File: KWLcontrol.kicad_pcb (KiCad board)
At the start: 2 copper layers, 56.4 x 38.5 mm, 33 parts, among them J1 Conn_01x03_Pin, J2 Conn_01x03_Socket, J3 Conn_01x03, U1 ESP32-WROOM-32, U2 TPS62172DSG, U3 TPS62172DSG, U4 TXS0101DBV

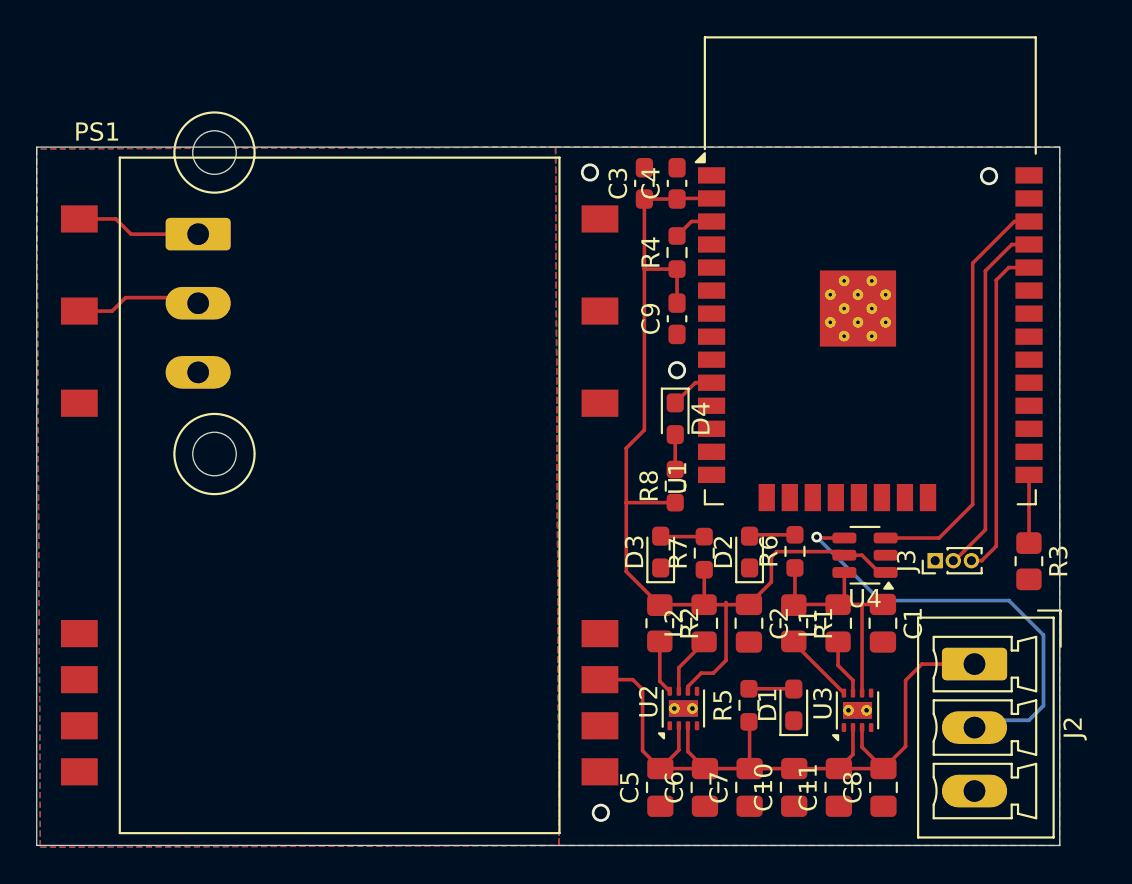
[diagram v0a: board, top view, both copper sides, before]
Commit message: new connectors, some silkscreen
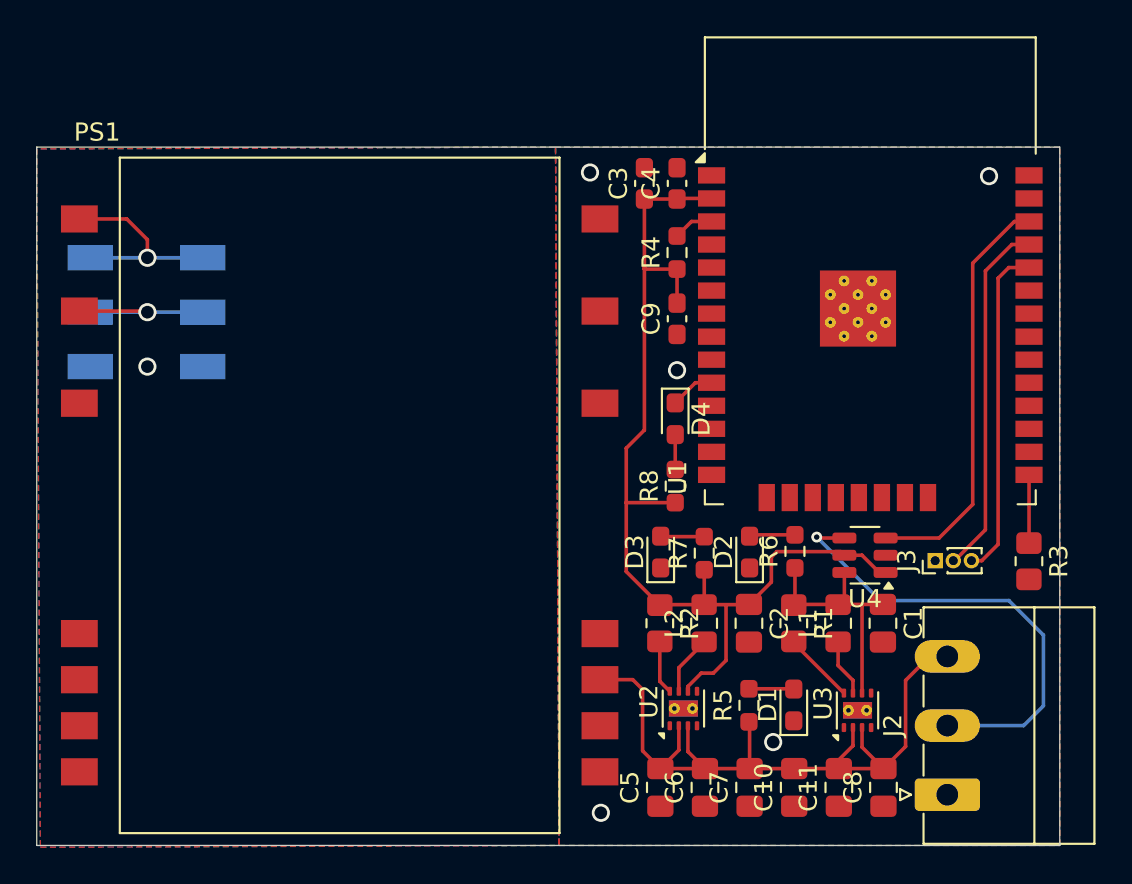
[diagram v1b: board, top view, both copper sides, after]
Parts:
- removed J1: Conn_01x03_Pin, Connector_Phoenix_MC:PhoenixContact_MC_1,5_3-GF-3.81_1x03_P3.81mm_Horizontal_ThreadedFlange_MountHole
- added J4: 2059-323/998-403, KWLcontrol:CONN3_2059-323&slash_998-403_WAG, B.Cu at (117.1, 117.4)
- J2: footprint Connector_Phoenix_MC:PhoenixContact_MCV_1,5_3-G-3.5_1x03_P3.50mm_Vertical -> Connector_Phoenix_MC:PhoenixContact_MC_1,5_3-G-3.81_1x03_P3.81mm_Horizontal
- moved J2 7.35 mm to (161.5, 144.0), turned to 90 degrees
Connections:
- J2 pad 1: +12V -> GNDREF
- J2 pad 3: GNDREF -> +12V
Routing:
- net /AC_L: track 6.90 -> 11.4 mm, vias 0 -> 1
- net /AC_N: track 6.86 -> 9.97 mm, vias 0 -> 1
- net Net-(J2-Pin_2): track 23.5 -> 25.9 mm
- net GNDREF: vias 4 -> 5
- net /AC_PE: vias 0 -> 1
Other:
- board text added: "12V"
- board text added: "DANGER HIGH VOLTAGE"
- board text added: "ESPHome home ventilation system control V1 Dr. Martin Schütz ms@mschuetz.com"
- board text added: "GND"
- board text added: "IN: 85 - 305 Volt AC"
- board text added: "L / Phase"
- board text added: "N / Neutral"
- board text added: "PE / Earth"
- board text added: "PWM"
- board text removed: "ESPHome home ventilation systetecontroll Dr. Martin Schütz ms@mschuetz.com"
